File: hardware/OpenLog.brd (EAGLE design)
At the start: 15.2 x 19.1 mm, 26 parts, among them Q1 16MHZ, U1 ATMEGA328P_TQFP, U2 3.3V MIC5205, U3 microSD Socket

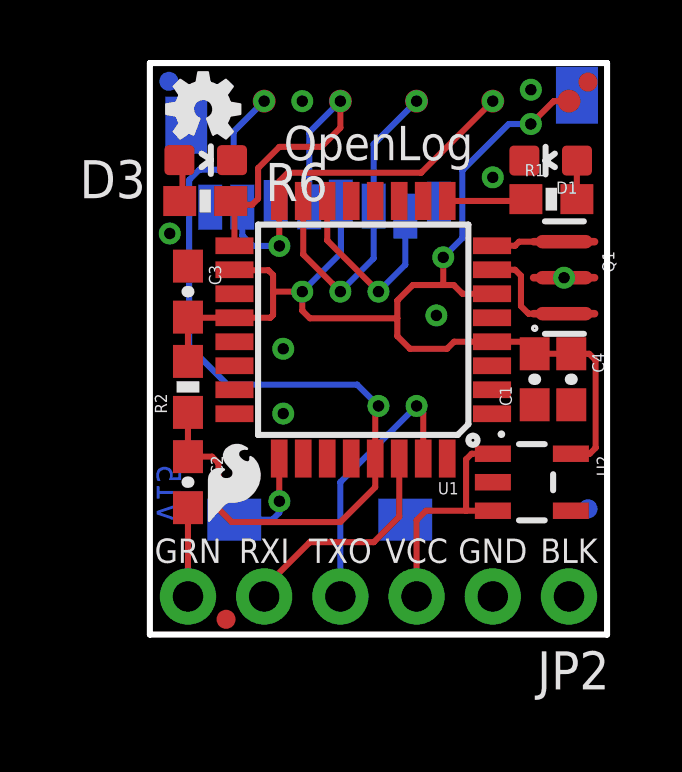
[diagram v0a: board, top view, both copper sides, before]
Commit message: moved 1 fiducial
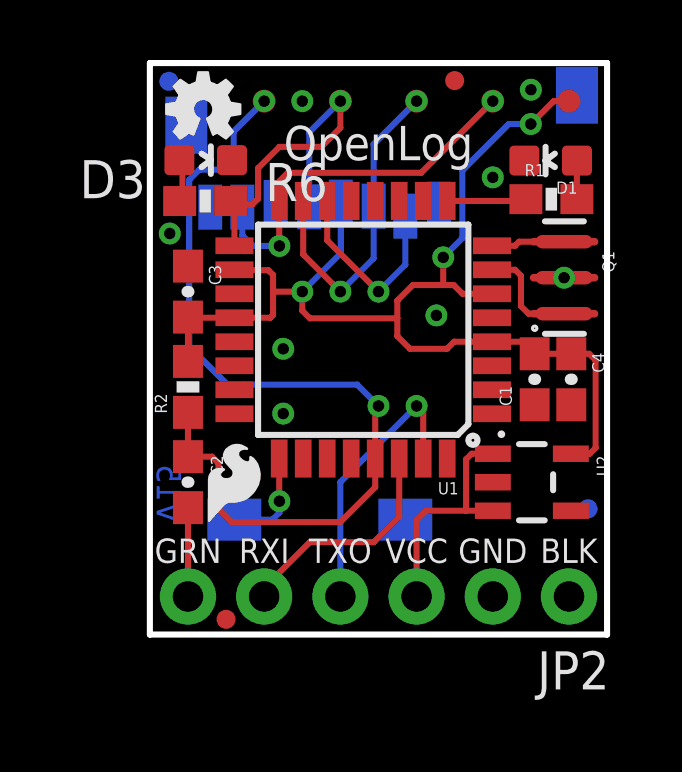
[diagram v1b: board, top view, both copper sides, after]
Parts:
- moved FID1 4.45 mm to (10.2, 18.5)

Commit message: moved bottom side fiducial
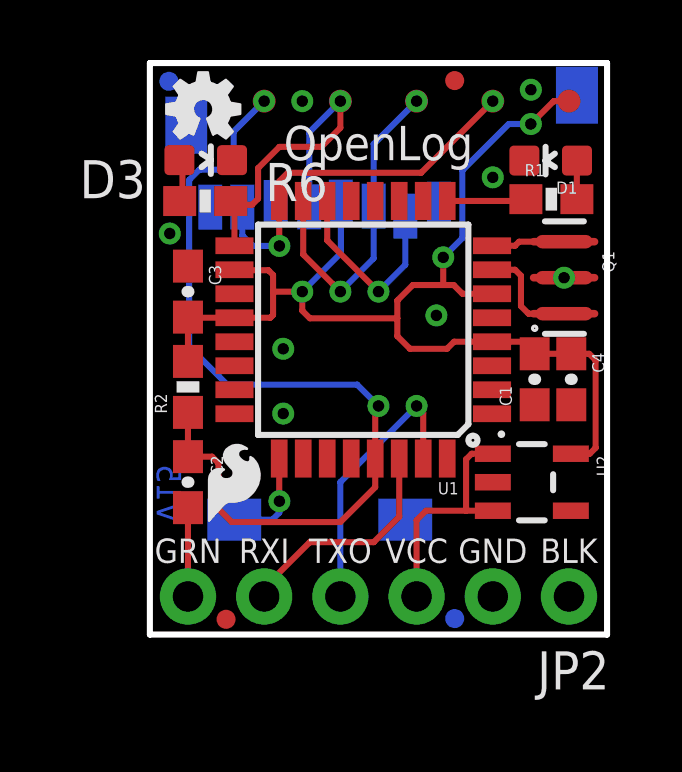
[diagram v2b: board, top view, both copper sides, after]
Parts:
- moved FID3 5.76 mm to (10.2, 0.53)
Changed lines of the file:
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@@
 <element name="TP1" library="SparkFun-Passives" package="PAD.03X.03" value="TEST-POINT3" x="13.97" y="17.78"/>
 <element name="LOGO2" library="SparkFun-Aesthetics" package="OSHW-LOGO-MINI" value="OSHW-LOGOMINI" x="1.778" y="17.526"/>
-<element name="FID3" library="SparkFun-Aesthetics" package="MICRO-FIDUCIAL" value="FIDUCIALUFIDUCIAL" x="14.605" y="4.191" rot="MR0"/>
+<element name="FID3" library="SparkFun-Aesthetics" package="MICRO-FIDUCIAL" value="FIDUCIALUFIDUCIAL" x="10.16" y="0.5334" rot="MR0"/>
 <element name="FID4" library="SparkFun-Aesthetics" package="MICRO-FIDUCIAL" value="FIDUCIALUFIDUCIAL" x="0.635" y="18.4404" rot="MR0"/>
 <element name="TP2" library="SparkFun-Passives" package="PAD.03X.03" value="TEST-POINT3" x="11.43" y="17.78" rot="R270"/>
